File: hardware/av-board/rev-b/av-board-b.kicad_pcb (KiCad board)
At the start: 4 copper layers, 94.6 x 69.4 mm, 167 parts, among them J1 RCA Y, J10 2x20 socket, J2 RCA Pb, J3 RCA Pr, J4 RCA L, J5 RCA R, J6 HDMI-001, J9 2x20 socket, SW1 TS-1187A-B-A-B, SW2 TS-1187A-B-A-B, U1 ADV7181DBCPZ-RL, U10 TPD4E05U06DQAR, U11 TPD4E05U06DQAR, U2 ADV7511KSTZ, U3 PCM1808PWR, U4 TLV62569DBVR, U5 TPS7A7001DDAR, U6 TPS7A7001DDAR, U7 TPS7A7001DDAR, U8 TPD4E05U06DQAR, U9 TPD4E05U06DQAR, Y1 28.63636MHz 20pF

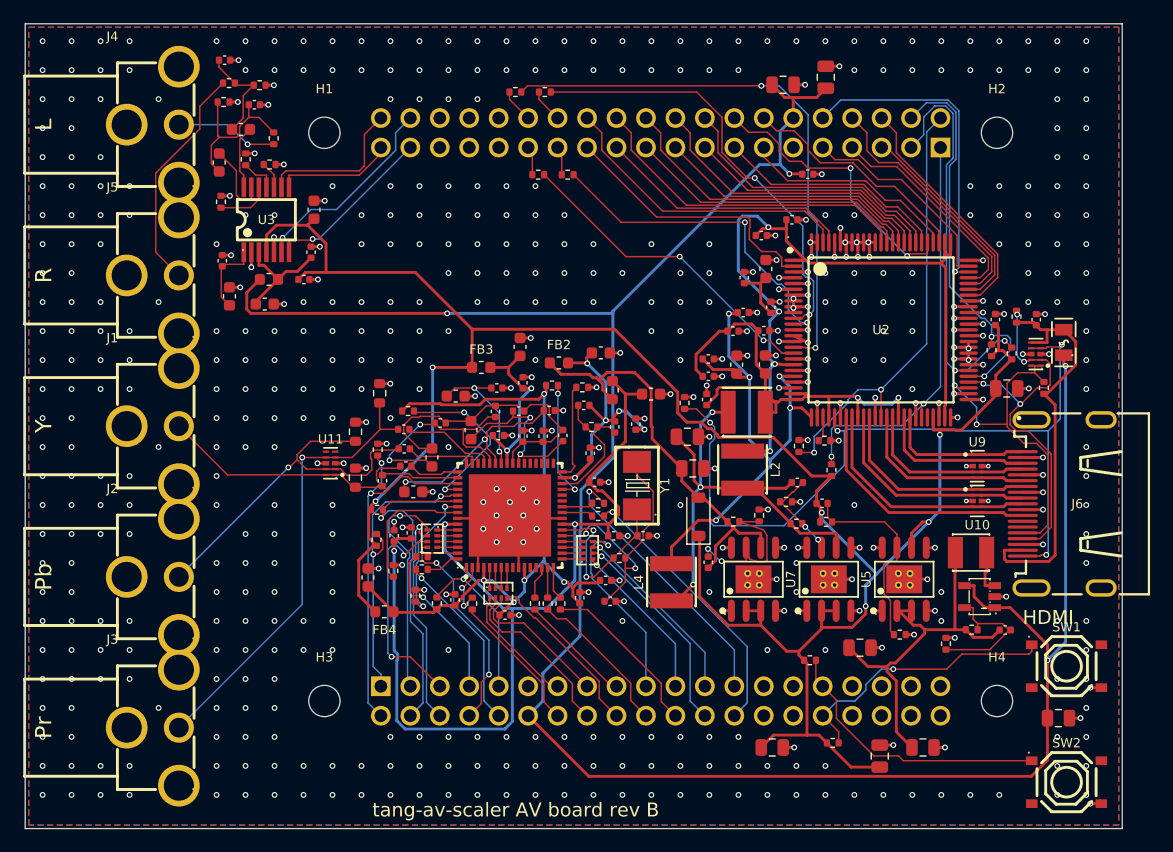
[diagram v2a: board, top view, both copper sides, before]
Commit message: AV boards: second full review, ESD at the connectors, rev C, rev B and C-B routed
Rev C (the SOM on its own carrier, C-A with the ADV7511, C-B with the SN65DP159) joins rev B on
shared code: kit/circuits.py (rev B's circuits), kit/adv7181d_layout.py, kit/tmds_layout.py,
rev-c/ (carrier, floor plan, SOM pin matching, design notes, review).

Review fixes (rev-b/review.md, rev-c/review.md):
- ESD at each connector: a TPD1E05U06 per video and S/PDIF input (the shared four-line arrays
  sat 11-25 mm from some of their connectors); every ESD part placed first, at its connector;
  an array's ground through the package to one via away from the connector (TI's layout); the
  VGA array's channels in the header's order; rev C's USB-C TVS between receptacle and fuse.
- XIAO: an ESP32-C3 boots right (SCK pulled up for GPIO8, TMS on D0 for GPIO2, 470 R on the
  translator's outputs for GPIO9's BOOT button).
- Rev B: J10 pins 29/30 (the Console's SDRAM EXIO pins, which a MiSTer-style fit puts on 3.3 V
  and GND) left open.
- D6 drawn as the unidirectional TVS it is.

Kit: plane vias never in pads, by true circle-to-box distance; analog lines and references kept
0.5 mm from digital ones by the router (Freerouting class-to-class rules); rip-up in the
finisher, kept only when it leaves fewer gaps; xtalk.py counts each close run once.

Rev B and C-B: routed, DRC clean, no unconnected items; schematics, fab files and renders
regenerated. C-A's routed board follows.

Co-Authored-By: Claude Opus 5.5 <noreply@anthropic.com>
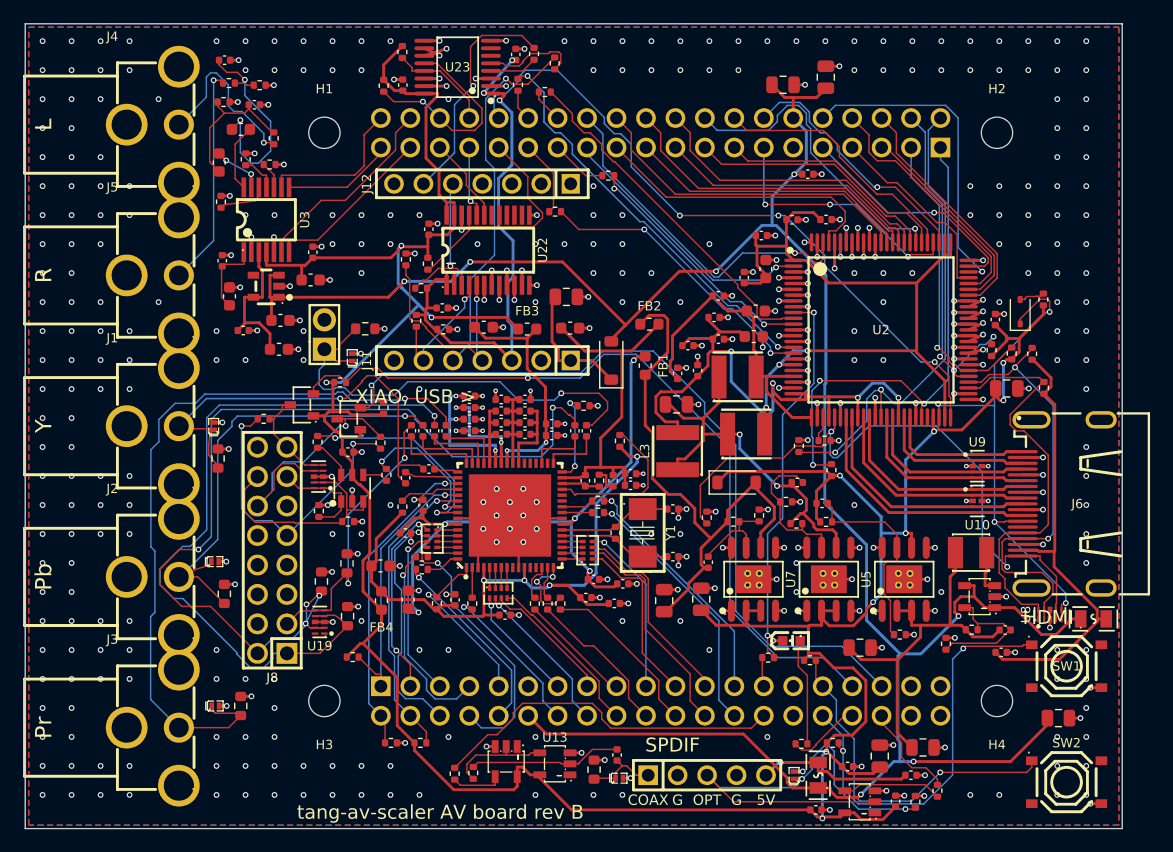
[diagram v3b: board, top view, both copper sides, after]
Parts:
- removed FB5: 120R, Inductor_SMD:L_0603_1608Metric
- removed U11: TPD4E05U06DQAR, lcsc:USON-10_L2.5-W1.0-P0.50-BL
- added C77: 100n, Capacitor_SMD:C_0402_1005Metric, F.Cu at (149.3, 87.6)
- added C78: 10u, Capacitor_SMD:C_0603_1608Metric, F.Cu at (138.1, 41.7)
- added C79: 10u, Capacitor_SMD:C_0603_1608Metric, F.Cu at (137.0, 47.6)
- added C80: 10u, Capacitor_SMD:C_0603_1608Metric, F.Cu at (137.2, 45.4)
- added C81: 100n, Capacitor_SMD:C_0402_1005Metric, F.Cu at (137.7, 38.9)
- added C82: 100n, Capacitor_SMD:C_0402_1005Metric, F.Cu at (140.3, 37.5)
- added C83: 100n, Capacitor_SMD:C_0402_1005Metric, F.Cu at (136.2, 42.5)
- added C84: 100n, Capacitor_SMD:C_0402_1005Metric, F.Cu at (143.3, 37.5)
- added C85: 100n, Capacitor_SMD:C_0402_1005Metric, F.Cu at (134.0, 47.8)
- added C86: 100n, Capacitor_SMD:C_0402_1005Metric, F.Cu at (132.2, 50.5)
- added C87: 100n, Capacitor_SMD:C_0402_1005Metric, F.Cu at (133.6, 45.9)
- added C88: 100n, Capacitor_SMD:C_0402_1005Metric, F.Cu at (131.3, 48.4)
- added C89: 100n, Capacitor_SMD:C_0402_1005Metric, F.Cu at (134.0, 44.1)
- added C90: 100n, Capacitor_SMD:C_0402_1005Metric, F.Cu at (130.5, 50.7)
- added C91: 100n, Capacitor_SMD:C_0402_1005Metric, F.Cu at (157.9, 46.1)
- added C92: 100n, Capacitor_SMD:C_0402_1005Metric, F.Cu at (158.4, 74.8)
- added D10: TPD1E05U06DPYR, lcsc:X1SON-2_L1.0-W0.6-P0.65-RD-1, F.Cu at (90.6, 79.4)
- added D11: TPD1E05U06DPYR, lcsc:X1SON-2_L1.0-W0.6-P0.65-RD-1, F.Cu at (102.4, 49.4)
- added D12: TPD1E05U06DPYR, lcsc:X1SON-2_L1.0-W0.6-P0.65-RD-1, F.Cu at (125.4, 85.7)
- added D13: TPD1E05U06DPYR, lcsc:X1SON-2_L1.0-W0.6-P0.65-RD-1, F.Cu at (140.5, 85.4)
- added D2: KT-0603R, lcsc:LED-SMD_L1.6-W0.8-R-RD, F.Cu at (140.3, 73.8)
- added D3: B5819W, Diode_SMD:D_SOD-123, F.Cu at (124.7, 49.6)
- added D7: 1N4148WS, Diode_SMD:D_SOD-323, F.Cu at (160.0, 45.4)
- added D8: TPD1E05U06DPYR, lcsc:X1SON-2_L1.0-W0.6-P0.65-RD-1, F.Cu at (90.5, 55.3)
- added D9: TPD1E05U06DPYR, lcsc:X1SON-2_L1.0-W0.6-P0.65-RD-1, F.Cu at (90.6, 67.0)
- added F2: 0.2A, lcsc:F0805, F.Cu at (166.3, 71.9)
- added J11: XIAO 5V..D7, lcsc:HDR-TH_7P-P2.54-V-F, F.Cu at (113.6, 49.6)
- added J12: XIAO D0..D6, lcsc:HDR-TH_7P-P2.54-V-F, F.Cu at (113.6, 34.4)
- added J13: SPDIF, lcsc:HDR-TH_5P-P2.54-V-M, F.Cu at (133.0, 85.4)
- added J7: SYNC, lcsc:HDR-TH_2P-P2.54-V-M, F.Cu at (100.0, 47.4)
- added J8: VGA, lcsc:HDR-TH_16P-P2.54-V-M-R2-C8-S2.54, F.Cu at (95.5, 66.0)
- added Q1: 2N7002, lcsc:SOT-23-3_L2.9-W1.3-P1.90-LS2.4-BR, F.Cu at (102.1, 54.7)
- added Q2: 2N7002, lcsc:SOT-23-3_L2.9-W1.3-P1.90-LS2.4-BR, F.Cu at (98.1, 53.5)
- added R52: 47k, Resistor_SMD:R_0402_1005Metric, F.Cu at (94.8, 54.7)
- added R53: 10k, Resistor_SMD:R_0402_1005Metric, F.Cu at (95.3, 32.7)
- added R54: 10k, Resistor_SMD:R_0402_1005Metric, F.Cu at (93.2, 32.3)
- added R55: 10k, Resistor_SMD:R_0402_1005Metric, F.Cu at (91.1, 36.0)
- added R56: 12k, Resistor_SMD:R_0402_1005Metric, F.Cu at (95.6, 30.5)
- added R57: 10k, Resistor_SMD:R_0402_1005Metric, F.Cu at (91.3, 27.3)
- added R58: 12k, Resistor_SMD:R_0402_1005Metric, F.Cu at (91.8, 25.7)
- added R59: 10k, Resistor_SMD:R_0402_1005Metric, F.Cu at (94.4, 25.9)
- added R60: 75, Resistor_SMD:R_0603_1608Metric, F.Cu at (123.3, 84.9)
- added R61: 1M, Resistor_SMD:R_0402_1005Metric, F.Cu at (112.8, 85.2)
- added R62: 33, Resistor_SMD:R_0402_1005Metric, F.Cu at (111.2, 85.3)
- added R63: 100k, Resistor_SMD:R_0402_1005Metric, F.Cu at (151.0, 87.7)
- added R64: 33, Resistor_SMD:R_0402_1005Metric, F.Cu at (152.9, 86.7)
- added R65: 49.9, Resistor_SMD:R_0402_1005Metric, F.Cu at (119.0, 26.5)
- added R66: 49.9, Resistor_SMD:R_0402_1005Metric, F.Cu at (116.7, 25.9)
- added R67: 49.9, Resistor_SMD:R_0402_1005Metric, F.Cu at (119.9, 36.8)
- added R68: 49.9, Resistor_SMD:R_0402_1005Metric, F.Cu at (124.5, 33.7)
- added R69: 49.9, Resistor_SMD:R_0402_1005Metric, F.Cu at (138.3, 75.3)
- added R70: 887, Resistor_SMD:R_0402_1005Metric, F.Cu at (143.1, 56.5)
- added R71: 2k, Resistor_SMD:R_0402_1005Metric, F.Cu at (157.5, 48.7)
- added R72: 2k, Resistor_SMD:R_0402_1005Metric, F.Cu at (159.3, 49.0)
- added R73: 2k, Resistor_SMD:R_0402_1005Metric, F.Cu at (143.7, 59.1)
- added R74: 2k, Resistor_SMD:R_0402_1005Metric, F.Cu at (140.9, 57.0)
- added R75: 2k, Resistor_SMD:R_0402_1005Metric, F.Cu at (162.1, 52.0)
- added R76: 2k, Resistor_SMD:R_0402_1005Metric, F.Cu at (161.0, 49.1)
- added R77: 10k, Resistor_SMD:R_0402_1005Metric, F.Cu at (133.0, 63.2)
- added R78: 27k, Resistor_SMD:R_0402_1005Metric, F.Cu at (162.0, 44.4)
- added U12: TPS7A2045PDBVR, lcsc:SOT-23-5_L2.9-W1.6-P0.95-LS2.8-BR, F.Cu at (95.0, 43.2)
- added U13: SN74LVC1GU04DBVR, lcsc:SOT-23-5_L3.0-W1.7-P0.95-LS2.8-BR, F.Cu at (119.9, 84.4)
- added U14: SN74LVC1G04DBVR, lcsc:SOT-23-5_L3.0-W1.7-P0.95-LS2.8-BR, F.Cu at (115.7, 84.2)
- added U15: SN74LVC1G04DBVR, lcsc:SOT-23-5_L3.0-W1.7-P0.95-LS2.8-BR, F.Cu at (146.2, 87.7)
- added U19: TPD4E05U06DQAR, lcsc:USON-10_L2.5-W1.0-P0.50-BL, F.Cu at (99.6, 72.2)
- added U20: TPD4E05U06DQAR, lcsc:USON-10_L2.5-W1.0-P0.50-BL, F.Cu at (99.5, 59.6)
- added U21: SN74LVC2G17DBVR, lcsc:SOT-23-6_L2.9-W1.6-P0.95-LS2.8-BL, F.Cu at (102.4, 60.6)
- added U22: SN74LVC8T245PWR, lcsc:TSSOP-24_L7.8-W4.4-P0.65-LS6.4-BL, F.Cu at (114.1, 40.1)
- added U23: SN74AVC4T245PWR, lcsc:TSSOP-16_L5.0-W4.4-P0.65-LS6.4-BL, F.Cu at (111.5, 24.3)
- C11: value 10u -> 6.8p; footprint Capacitor_SMD:C_0805_2012Metric -> Capacitor_SMD:C_0402_1005Metric
- C12, C15, C9: value 220p -> 10u; footprint Capacitor_SMD:C_0402_1005Metric -> Capacitor_SMD:C_0805_2012Metric
- C14: value 10u -> 220p; footprint Capacitor_SMD:C_0805_2012Metric -> Capacitor_SMD:C_0402_1005Metric
- C16, C18, C19: footprint Capacitor_SMD:C_0603_1608Metric -> Capacitor_SMD:C_0805_2012Metric
- C17, C20: value 10u -> 220p; footprint Capacitor_SMD:C_0603_1608Metric -> Capacitor_SMD:C_0402_1005Metric
- C23, C24, C66, C68: value 100n -> 10u; footprint Capacitor_SMD:C_0402_1005Metric -> Capacitor_SMD:C_0603_1608Metric
- C26: value 1n -> 100n
- C27: value 33p -> 100n
- C28: value 33p -> 1n
- C29: value 100n -> 1n
- C30: value 100n -> 33p
- C31: value 10u -> 33p; footprint Capacitor_SMD:C_0603_1608Metric -> Capacitor_SMD:C_0402_1005Metric
- C33, C46, C48, C50, C52, C54: value 10n -> 100n
- C34, C37: footprint Capacitor_SMD:C_0603_1608Metric -> Capacitor_SMD:C_0402_1005Metric
- C39: value 10u -> 10n; footprint Capacitor_SMD:C_0603_1608Metric -> Capacitor_SMD:C_0402_1005Metric
- C40: value 100n -> 10u
- C41: value 82n -> 100n
- C42: value 10n -> 10u
- C44: value 10n -> 82n
- C45, C51, C53, C55, C57, C59: value 100n -> 10n
- C5, C7, C8: value 10u -> 100n; footprint Capacitor_SMD:C_0805_2012Metric -> Capacitor_SMD:C_0402_1005Metric
- C56, C58, C60: value 10u -> 100n; footprint Capacitor_SMD:C_0603_1608Metric -> Capacitor_SMD:C_0402_1005Metric
- C6: value 6.8p -> 100n
- C61: value 220p -> 10n
- C63: value 220p -> 100n
- C64: value 1u -> 10u
- C69, C71: value 100n -> 220p
- C70, C72: value 100n -> 1u; footprint Capacitor_SMD:C_0402_1005Metric -> Capacitor_SMD:C_0603_1608Metric
- R10, R8: value 30.1k -> 10k
- R11, R12: value 75 -> 10k; footprint Resistor_SMD:R_0603_1608Metric -> Resistor_SMD:R_0402_1005Metric
- R13: value 75 -> 499k; footprint Resistor_SMD:R_0603_1608Metric -> Resistor_SMD:R_0402_1005Metric
- R14: value 1M -> 100k
- R15: value 1.69k -> 169k
- R16, R18, R20: value 33 -> 30.1k
- R17, R19: value 33 -> 78.7k
- R21, R22, R23: value 33 -> 75; footprint Resistor_SMD:R_0402_1005Metric -> Resistor_SMD:R_0603_1608Metric
- R24: value 4.7k -> 75; footprint Resistor_SMD:R_0402_1005Metric -> Resistor_SMD:R_0603_1608Metric
- R25: value 4.7k -> 1M
- R26: value 4.7k -> 1.69k
- R27, R28, R29: value 4.7k -> 33
- R3: value 499k -> 470
- R30, R31, R32, R33, R34: value 10k -> 33
- R35, R36, R37, R38, R39, R51: value 10k -> 4.7k
- R40: value 49.9 -> 4.7k
- R41: value 49.9 -> 10k
- R42, R43: value 49.9 -> 75; footprint Resistor_SMD:R_0402_1005Metric -> Resistor_SMD:R_0603_1608Metric
- R44: value 887 -> 75; footprint Resistor_SMD:R_0402_1005Metric -> Resistor_SMD:R_0603_1608Metric
- R45, R46: value 2k -> 10k
- R47, R48: value 2k -> 33
- R49: value 2k -> 4.7k
- R5: value 169k -> 470
- R50: value 2k -> 47k
- R6: value 30.1k -> 470
- R7, R9: value 78.7k -> 10k
- moved C7 69.3 mm to (116.5, 23.2), turned to 90 degrees
- moved C6 60.5 mm to (109.0, 38.3), turned to 90 degrees
- moved R45 59.6 mm to (99.5, 62.6)
- moved R46 59.0 mm to (102.0, 63.5), turned to 0 degrees
- moved C8 58.3 mm to (106.8, 25.9), turned to 90 degrees
- moved R6 57.6 mm to (119.9, 24.0), turned to 90 degrees
- moved R37 57.1 mm to (105.7, 82.6)
- moved R49 57.0 mm to (105.1, 53.7)
- moved R50 55.9 mm to (104.8, 56.7)
- moved C4 55.9 mm to (120.9, 44.2)
- moved R13 55.0 mm to (155.8, 72.9), turned to 0 degrees
- moved R4 51.1 mm to (110.2, 47.0), turned to 0 degrees
- moved C71 49.8 mm to (91.4, 23.7)
- moved R35 49.7 mm to (108.3, 82.6), turned to 0 degrees
- moved R38 48.3 mm to (109.7, 70.6), turned to 90 degrees
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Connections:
- C10 pad 1: 3V3 -> 3V6
- C11 pad 1: 1V8A -> 3V6
- C11 pad 2: GND -> FB_3V6
- C12 pad 1: 1V8A -> 3V6
- C12 pad 2: FB_1V8A -> GND
- C14 pad 1: 1V8B -> 3V3
- C14 pad 2: GND -> FB_3V3
- C15 pad 1: 1V8B -> 3V3
- C15 pad 2: FB_1V8B -> GND
- C16 pad 1: AV_DVDD -> 1V8A
- C17 pad 1: AV_PVDD -> 1V8A
- C17 pad 2: GND -> FB_1V8A
- C18 pad 1: AV_AVDD -> 3V3
- C19 pad 1: AV_DVDDIO -> 1V8B
- C20 pad 1: TX_DVDD -> 1V8B
- C20 pad 2: GND -> FB_1V8B
- C21 pad 1: TX_AVDD -> AV_DVDD
- C22 pad 1: TX_PLVDD -> AV_PVDD
- C23 pad 1: RCA_Y -> AV_AVDD
- C23 pad 2: AIN_Y -> GND
- C24 pad 1: RCA_PB -> AV_DVDDIO
- C24 pad 2: AIN_PB -> GND
- C25 pad 1: RCA_PR -> RCA_Y
- C25 pad 2: AIN_PR -> AIN_Y
- C26 pad 1: RCA_Y -> RCA_PB
- C26 pad 2: SYNC_Y -> AIN_PB
- C27 pad 1: XTAL -> RCA_PR
- C27 pad 2: GND -> AIN_PR
- C28 pad 1: XTAL1 -> RCA_Y
- C28 pad 2: GND -> SYNC_Y
- C29 pad 1: CAPY2 -> RCA_SYNC
- C29 pad 2: GND -> SYNC_G
- C30 pad 1: CAPY2 -> XTAL
- C31 pad 1: CAPY1 -> XTAL1
- C31 pad 2: CAPY2 -> GND
- C32 pad 1: CAPY1 -> CAPY2
- C32 pad 2: CAPY2 -> GND
- C33 pad 1: CAPY1 -> CAPY2
- C33 pad 2: CAPY2 -> GND
- C34 pad 1: CAPC2 -> CAPY1
- C35 pad 1: CAPC2 -> CAPY1
- C36 pad 1: CAPC2 -> CAPY1
- C37 pad 1: REFOUT -> CAPC2
- C37 pad 2: GND -> CAPY2
- C38 pad 1: REFOUT -> CAPC2
- C38 pad 2: GND -> CAPY2
- C39 pad 1: CML -> CAPC2
- C39 pad 2: GND -> CAPY2
- C4 pad 1: +5V -> XIAO_5V
- C40 pad 1: CML -> REFOUT
- C41 pad 1: ELPF_RC -> REFOUT
- C41 pad 2: AV_PVDD -> GND
- C42 pad 1: ELPF -> CML
- C42 pad 2: AV_PVDD -> GND
- C43 pad 1: AV_DVDDIO -> CML
- C44 pad 1: AV_DVDDIO -> ELPF_RC
- C44 pad 2: GND -> AV_PVDD
- C45 pad 1: AV_DVDDIO -> ELPF
- C45 pad 2: GND -> AV_PVDD
- C46 pad 1: AV_DVDDIO -> VGA_R
- C46 pad 2: GND -> AIN_VR
- C47 pad 1: AV_DVDD -> VGA_G
- C47 pad 2: GND -> AIN_VG
- C48 pad 1: AV_DVDD -> VGA_B
- C48 pad 2: GND -> AIN_VB
- C49 pad 1: AV_DVDD -> 3V3
- C5 pad 1: 3V6 -> XIAO_3V3
- C50 pad 1: AV_DVDD -> AV_DVDDIO
- C51 pad 1: AV_PVDD -> AV_DVDDIO
- C52 pad 1: AV_PVDD -> AV_DVDDIO
- C53 pad 1: AV_AVDD -> AV_DVDDIO
- C54 pad 1: AV_AVDD -> AV_DVDD
- C55 pad 1: VREF -> AV_DVDD
- C56 pad 1: VREF -> AV_DVDD
- C57 pad 1: 5VA -> AV_DVDD
- C58 pad 1: 5VA -> AV_PVDD
- C59 pad 1: 3V3 -> AV_PVDD
- C6 pad 1: 3V6 -> 3V3
- C6 pad 2: FB_3V6 -> GND
- C60 pad 1: 3V3 -> AV_AVDD
- C61 pad 1: AUD_DIV_L -> AV_AVDD
- C62 pad 1: AUD_DIV_L -> +5V
- C62 pad 2: AUD_VINL -> GND
- C63 pad 1: AUD_DIV_R -> VREF
- C64 pad 1: AUD_DIV_R -> VREF
- C64 pad 2: AUD_VINR -> GND
- C65 pad 1: TX_DVDD -> 5VA
- C66 pad 1: TX_DVDD -> 5VA
- C67 pad 1: TX_DVDD -> 3V3
- C68 pad 1: TX_DVDD -> 3V3
- C69 pad 1: TX_AVDD -> AUD_DIV_L
- C7 pad 1: 3V6 -> XIAO_3V3
- C70 pad 1: TX_AVDD -> AUD_DIV_L
- C70 pad 2: GND -> AUD_VINL
- C71 pad 1: TX_AVDD -> AUD_DIV_R
- C72 pad 1: TX_AVDD -> AUD_DIV_R
- C72 pad 2: GND -> AUD_VINR
- C73 pad 1: TX_PLVDD -> SPDIF_5V
- C74 pad 1: TX_PLVDD -> SPDIF_COAX
- C74 pad 2: GND -> SPDIF_AC
- C76 pad 1: HDMI_5V -> 3V3
- C9 pad 1: 3V3 -> +5V
- C9 pad 2: FB_3V3 -> GND
- F1 pad 2: HDMI_5V -> SPDIF_5V
- J10 pad 27: GND -> SPDIF_RX
- J10 pad 28: GND -> OUT_SPDIF
- J10 pad 29: GND -> (no net)
- J10 pad 30: GND -> (no net)
- J10 pad 33: GND -> IN_LED
- J10 pad 34: GND -> VGA_SCL_F
- J10 pad 35: GND -> SPDIF_ORX
- J10 pad 36: GND -> VGA_SDA_F
- J6 pad 13: (no net) -> HDMI_CEC
- J9 pad 31: GND -> OUT_CECCLK
- J9 pad 32: GND -> ESP_CS
- J9 pad 33: GND -> ESP_IRQ
- J9 pad 34: GND -> ESP_SCK
- J9 pad 35: GND -> ESP_MISO
- J9 pad 36: GND -> ESP_MOSI
- R10 pad 1: FB_1V8B -> ESP_CS
- R10 pad 2: GND -> 3V3
- R11 pad 1: RCA_Y -> ESP_IRQ
- R11 pad 2: GND -> 3V3
- R12 pad 1: RCA_PB -> ESP_MISO
- R12 pad 2: GND -> 3V3
- R13 pad 1: RCA_PR -> 3V6
- R13 pad 2: GND -> FB_3V6
- R14 pad 1: XTAL -> FB_3V6
- R14 pad 2: XTAL1 -> GND
- R15 pad 1: ELPF -> 3V3
- R15 pad 2: ELPF_RC -> FB_3V3
- R16 pad 1: AV_C7 -> FB_3V3
- R16 pad 2: IN_C7 -> GND
- R17 pad 1: AV_C6 -> 1V8A
- R17 pad 2: IN_C6 -> FB_1V8A
- R18 pad 1: AV_C5 -> FB_1V8A
- R18 pad 2: IN_C5 -> GND
- R19 pad 1: AV_C1 -> 1V8B
- R19 pad 2: IN_C1 -> FB_1V8B
- R20 pad 1: AV_C0 -> FB_1V8B
- R20 pad 2: IN_C0 -> GND
- R21 pad 1: AV_HS -> RCA_Y
- R21 pad 2: IN_HS -> GND
- R22 pad 1: AV_VS -> RCA_PB
- R22 pad 2: IN_VS -> GND
- R23 pad 1: AV_DE -> RCA_PR
- R23 pad 2: IN_DE -> GND
- R24 pad 1: 3V3 -> RCA_SYNC
- R24 pad 2: IN_SCL -> GND
- R25 pad 1: 3V3 -> XTAL
- R25 pad 2: IN_SDA -> XTAL1
- R26 pad 1: IN_RESET_N -> ELPF
- R26 pad 2: GND -> ELPF_RC
- R27 pad 1: AV_DVDDIO -> AV_C7
- R27 pad 2: IN_INT -> IN_C7
- R28 pad 1: AV_DVDDIO -> AV_C6
- R28 pad 2: ALSB -> IN_C6
- R29 pad 1: AV_DVDDIO -> AV_C5
- R29 pad 2: PWRDWN -> IN_C5
- R3 pad 1: 3V6 -> IN_LED
- R3 pad 2: FB_3V6 -> LED_A
- R30 pad 1: PD_FB -> AV_C1
- R30 pad 2: GND -> IN_C1
- R31 pad 1: PD_HS_IN_CS_IN -> AV_C0
- R31 pad 2: GND -> IN_C0
- R32 pad 1: PD_VS_IN -> AV_HS
- R32 pad 2: GND -> IN_HS
- R33 pad 1: MD0 -> AV_VS
- R33 pad 2: GND -> IN_VS
- R34 pad 1: MD1 -> AV_DE
- R34 pad 2: GND -> IN_DE
- R35 pad 1: FMT -> 3V3
- R35 pad 2: GND -> IN_SCL
- R36 pad 1: RCA_L -> 3V3
- R36 pad 2: AUD_DIV_L -> IN_SDA
- R37 pad 1: AUD_DIV_L -> IN_RESET_N
- R38 pad 1: RCA_R -> AV_DVDDIO
- R38 pad 2: AUD_DIV_R -> IN_INT
- R39 pad 1: AUD_DIV_R -> AV_DVDDIO
- R39 pad 2: GND -> ALSB
- R4 pad 1: FB_3V6 -> XIAO_3V3
- R40 pad 1: OUT_MCLK -> AV_DVDDIO
- R40 pad 2: TX_MCLK -> PWRDWN
- R41 pad 1: OUT_SCLK -> PD_FB
- R41 pad 2: TX_SCLK -> GND
- R42 pad 1: OUT_LRCLK -> VGA_R
- R42 pad 2: TX_LRCLK -> GND
- R43 pad 1: OUT_I2S0 -> VGA_G
- R43 pad 2: TX_I2S0 -> GND
- R44 pad 1: R_EXT -> VGA_B
- R45 pad 1: 3V3 -> VGA_HS
- R45 pad 2: OUT_SCL -> GND
- R46 pad 1: 3V3 -> VGA_VS
- R46 pad 2: OUT_SDA -> GND
- R47 pad 1: 3V3 -> VGA_HSB
- R47 pad 2: OUT_INT -> VGA_HSIN
- R48 pad 1: OUT_PD -> VGA_VSB
- R48 pad 2: GND -> VGA_VSIN
- R49 pad 1: HDMI_5V -> 3V3
- R49 pad 2: HDMI_SCL -> VGA_SDA_F
- R5 pad 1: 3V3 -> XIAO_D5_A
- R5 pad 2: FB_3V3 -> XIAO_D5
- R50 pad 1: HDMI_5V -> VGA_5V
- R50 pad 2: HDMI_SDA -> VGA_SDA
- R51 pad 1: HDMI_HPD -> 3V3
- R51 pad 2: GND -> VGA_SCL_F
- R6 pad 1: FB_3V3 -> XIAO_D9_A
- R6 pad 2: GND -> XIAO_D9
- R7 pad 1: 1V8A -> XIAO_D4
- R7 pad 2: FB_1V8A -> XIAO_3V3
- R8 pad 1: FB_1V8A -> XIAO_D8
- R8 pad 2: GND -> XIAO_3V3
- R9 pad 1: 1V8B -> XIAO_D10
- R9 pad 2: FB_1V8B -> GND
- U1 pad 33: (no net) -> SYNC_G
- U1 pad 35: (no net) -> AIN_VG
- U1 pad 46: (no net) -> AIN_VR
- U1 pad 48: (no net) -> AIN_VB
- U1 pad 55: PD_VS_IN -> VGA_VSIN
- U1 pad 56: PD_HS_IN_CS_IN -> VGA_HSIN
- U2 pad 10: GND -> TX_SPDIF
- U2 pad 48: GND -> HDMI_CEC
- U2 pad 50: GND -> OUT_CECCLK
- U8 pad 5: HDMI_5V -> HDMI_CEC
- U8 pad 6: HDMI_5V -> HDMI_CEC
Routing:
- net 3V3: track 194.3 -> 282.9 mm, vias 6 -> 11
- net VGA_G: track 0.00 -> 79.7 mm, vias 0 -> 5
- net VGA_SDA_F: track 0.00 -> 69.9 mm, vias 0 -> 1
- net VGA_SCL_F: track 0.00 -> 69.4 mm, vias 0 -> 1
- net VGA_R: track 0.00 -> 61.8 mm, vias 0 -> 1
- net OUT_CECCLK: track 0.00 -> 58.9 mm, vias 0 -> 3
- net GND: track 161.9 -> 220.4 mm, vias 584 -> 482
- net XIAO_3V3: track 0.00 -> 48.9 mm, vias 0 -> 3
- net HDMI_CEC: track 0.00 -> 44.7 mm, vias 0 -> 4
- net SPDIF_OPT: track 0.00 -> 40.6 mm, vias 0 -> 2
- net RCA_SYNC: track 0.00 -> 39.8 mm, vias 0 -> 1
- net TX_SPDIF: track 0.00 -> 33.4 mm, vias 0 -> 2
- net XIAO_D9: track 0.00 -> 32.2 mm, vias 0 -> 1
- net SPDIF_RX: track 0.00 -> 30.9 mm
- net AV_DVDD: track 82.2 -> 54.6 mm, vias 3 -> 5
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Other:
- board text added: "5V"
- board text added: "COAX"
- board text added: "G"
- board text added: "OPT"
- board text added: "SPDIF"
- board text added: "XIAO, USB >"

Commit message: AV boards: the last complete, valid design of each revision; decoupling at the pins
Each revision's board, schematic, fab files and renders are its last complete
route: DRC clean, no unconnected items, ERC clean, the board equal to its
schematic part for part (pads, values, footprints; only the mounting holes
H1-H4 have no symbol).

- Rev A: the silkscreen pass (labels clear of pads, texts and part bodies);
  copper unchanged.
- Rev B: the previous route with the silkscreen pass. Its schematic stays the
  one it was routed from: board.py now numbers eight capacitors the other way
  round, and its placement fixes (below) are not routed yet, the routes on the
  new placement having left 1 and 3 connections (review.md, Status).
- C-A: routed again on the fixed placement (try-ca-p1), the copper the router
  laid twice over taken up (218 segments).
- C-B: S/PDIF on rev B's 5-pin header instead of the coax jack, the HDMI
  receptacle next to the RCAs, the board 100 x 100 mm; routed again on the
  fixed placement (try-cb-p3). 5.4 mm of copper laid side by side in five
  nets is left (rev-c/review.md).

The review found decoupling not at the pins on every board (ADV7511 9-25 mm,
DP159 6-13 mm, the bucks' input capacitor by EN, the LDOs' capacitors, the
clock LDOs 73-80 mm from their chip) and C's VBUS_IN 0.25 mm wide for 2 A:
- parts.py: Part.at = "REF.PAD", the one pad a capacitor or filter serves;
  circuits, carrier.py and board.py name it for every regulator and supply pin
- pcbkit.py placer: ESD parts first, then small chips, then the at= capacitors
  and bias parts in board.py order; mean pin-to-capacitor distance on the
  placements: rev B 8.1 -> 3.6 mm, C-A 6.3 -> 3.3, C-B 5.5 -> 3.4
- rev C: VBUS_IN 0.7/1.2 mm into the TVS and fuse; rev B and C: the coax
  slicer placed first (SPDIF_AC a bias net); rev B: the buck U4 turned over

Kit: the silkscreen pass (labels clear of pads, texts, parts and the SOM,
reserved in the placer); prune takes up copper lying on another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
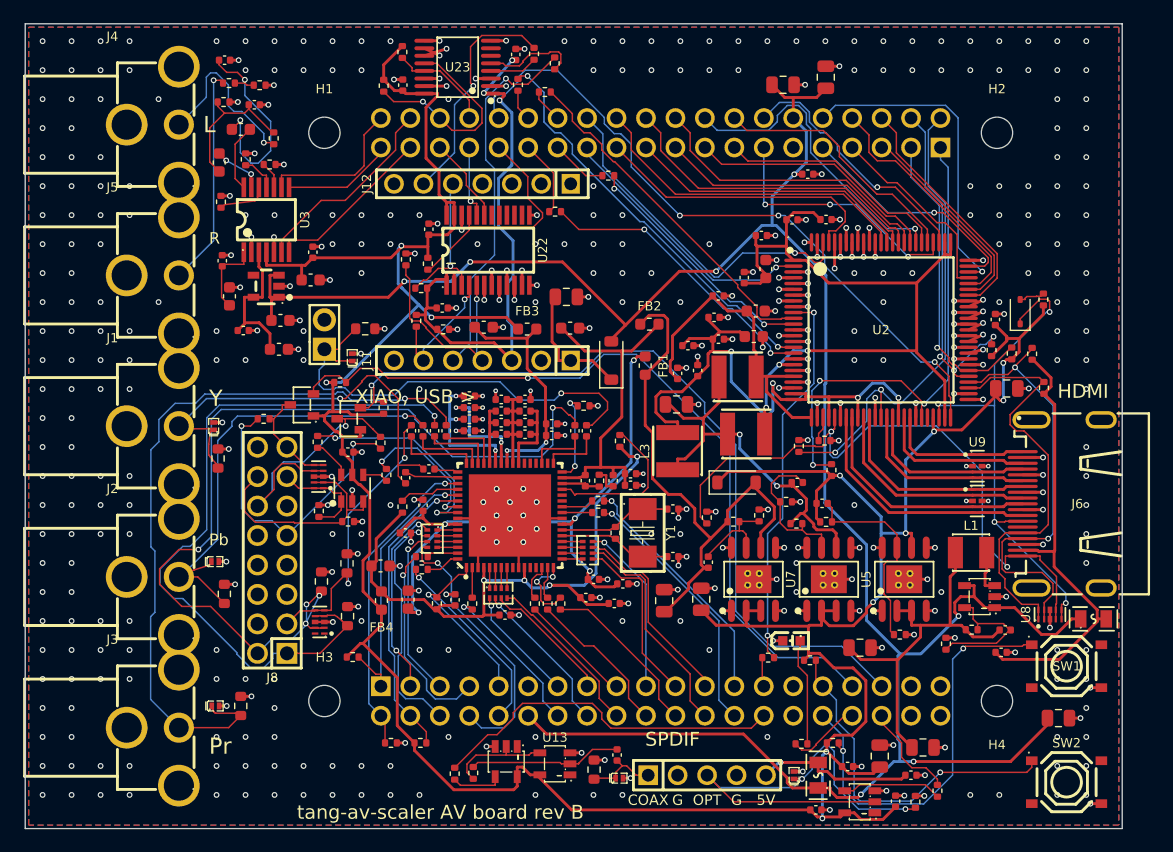
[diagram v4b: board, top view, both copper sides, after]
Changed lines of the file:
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@@
 		(tags "mountinghole M2.5")
 		(property "Reference" "H3"
-			(at 0 3.774999 0)
+			(at 0 -3.775 0)
 			(layer "F.SilkS")
 			(effects
@@
 		(at 166.3188 71.9207)
 		(property "Reference" "F2"
-			(at -0.000001 0 0)
+			(at 0 0 0)
 			(layer "F.SilkS")
 			(hide yes)
@@
 		(at 111.4887 24.3428 90)
 		(property "Reference" "U23"
-			(at 0 0 0)
+			(at 0.000001 0 0)
 			(layer "F.SilkS")
 			(effects
@@
 		(at 136.3643 55.9849)
 		(property "Reference" "L2"
-			(at 0 0 0)
+			(at 0 -0.000001 0)
 			(layer "F.SilkS")
 			(hide yes)
@@
 		(at 155.7635 66.2035)
 		(property "Reference" "L1"
-			(at 0 0 0)
+			(at 0 -2.325001 0)
 			(layer "F.SilkS")
-			(hide yes)
 			(effects
 				(font
@@
 		(at 156.3 61.75 -90)
 		(property "Reference" "U10"
-			(at 2.075 0 0)
+			(at 0 0 0)
 			(layer "F.SilkS")
+			(hide yes)
 			(effects
 				(font
@@
 		(at 99.5959 72.1852 90)
 		(property "Reference" "U19"
-			(at -2.075 0 0)
+			(at 0 0 0)
 			(layer "F.SilkS")
+			(hide yes)
 			(effects
 				(font
@@
 		(at 94.982 43.2327)
 		(property "Reference" "U12"
-			(at -0.000001 0 0)
+			(at 0 0 0)
 			(layer "F.SilkS")
 			(hide yes)
@@
 		(tags "inductor")
 		(property "Reference" "FB2"
-			(at 0 -1.555 0)
+			(at -0.000001 -1.555001 0)
 			(layer "F.SilkS")
 			(effects
@@
 		(tags "inductor")
 		(property "Reference" "FB1"
-			(at 0 1.554999 90)
+			(at 0 1.555 90)
 			(layer "F.SilkS")
 			(effects
@@
 		(at 146.1663 87.6932)
 		(property "Reference" "U15"
-			(at 0 0 0)
+			(at 0 -0.000001 0)
 			(layer "F.SilkS")
 			(hide yes)
@@
 		(at 115.6771 84.2241 90)
 		(property "Reference" "U14"
-			(at 0 -0.000001 0)
+			(at 0 0 0)
 			(layer "F.SilkS")
 			(hide yes)
@@
 		)
 	)
-	(gr_text "XIAO, USB >"
-		(at 107.865 52.765 0)
+	(gr_text "R"
+		(at 90.05 39.099999 0)
 		(layer "F.SilkS")
 		(effects
 			(font
-				(size 1.2 1.2)
-				(thickness 0.18)
+				(size 1 1)
+				(thickness 0.15)
 			)
+			(justify left)
 		)
 	)
-	(gr_text "tang-av-scaler AV board rev B"
-		(at 110 88.6 0)
+	(gr_text "Pb"
+		(at 90.05 65.099999 0)
 		(layer "F.SilkS")
 		(effects
 			(font
-				(size 1.2 1.2)
-				(thickness 0.18)
+				(size 1 1)
+				(thickness 0.15)
 			)
+			(justify left)
 		)
 	)
-	(gr_text "SPDIF"
-		(at 130.025 82.805 0)
+	(gr_text "XIAO, USB >"
+		(at 107.865 52.765 0)
 		(layer "F.SilkS")
 		(effects
@@
 		)
 	)
-	(gr_text "HDMI"
-		(at 162.42 71.8 0)
+	(gr_text "tang-av-scaler AV board rev B"
+		(at 110 88.6 0)
 		(layer "F.SilkS")
 		(effects
@@
 		)
 	)
-	(gr_text "L"
-		(at 75.8 29.3 90)
+	(gr_text "SPDIF"
+		(at 130.025 82.305 0)
 		(layer "F.SilkS")
 		(effects
 			(font
-				(size 1.4 1.4)
+				(size 1.2 1.2)
 				(thickness 0.18)
 			)
 		)
 	)
-	(gr_text "R"
-		(at 75.8 42.3 90)
+	(gr_text "HDMI"
+		(at 165.42 52.3 0)
 		(layer "F.SilkS")
 		(effects
 			(font
-				(size 1.4 1.4)
+				(size 1.2 1.2)
 				(thickness 0.18)
 			)
 		)
 	)
-	(gr_text "Y"
-		(at 75.8 55.3 90)
+	(gr_text "L"
+		(at 89.55 29.3 0)
 		(layer "F.SilkS")
 		(effects
@@
 				(thickness 0.18)
 			)
+			(justify left)
 		)
 	)
-	(gr_text "Pb"
-		(at 75.8 68.3 90)
+	(gr_text "Y"
+		(at 90.05 52.9 0)
 		(layer "F.SilkS")
 		(effects
@@
 				(thickness 0.18)
 			)
+			(justify left)
 		)
 	)
 	(gr_text "Pr"
-		(at 75.8 81.3 90)
+		(at 90.05 82.899999 0)
 		(layer "F.SilkS")
 		(effects
@@
 				(thickness 0.18)
 			)
+			(justify left)
 		)
 	)
